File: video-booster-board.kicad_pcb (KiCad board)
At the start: 4 copper layers, 40 x 41.5 mm, 143 parts, among them IC1 INA180A1IDBVT, J1 0473460001, J10 M20-9990246, J12 solder_jumper, J13 solder_jumper, J14 solder_jumper, J2 CHDMI-AMSS-01-C-Vertical, J3 CHDMI-AMSS-01-C-Vertical, J4 694103107102, J5 solder_jumper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

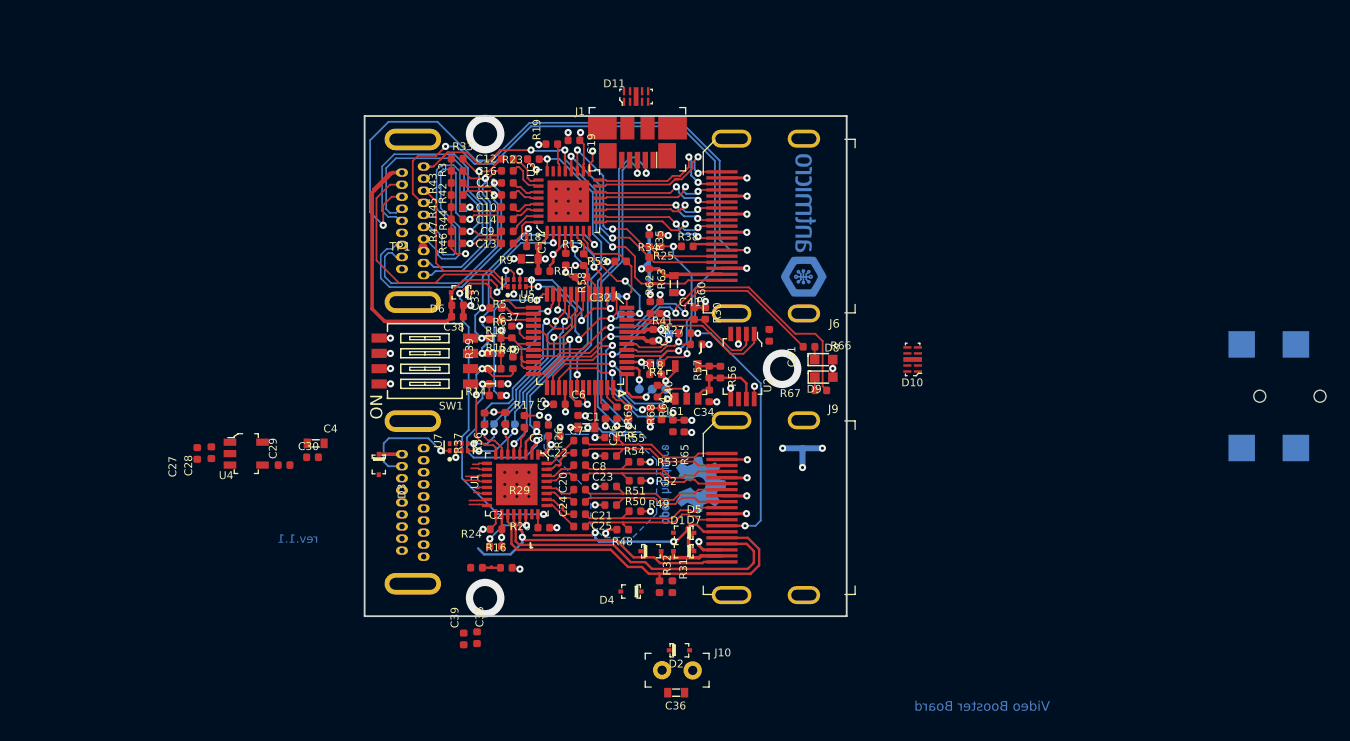
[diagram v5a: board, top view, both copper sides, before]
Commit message: Updated layout of 3V3 LDO
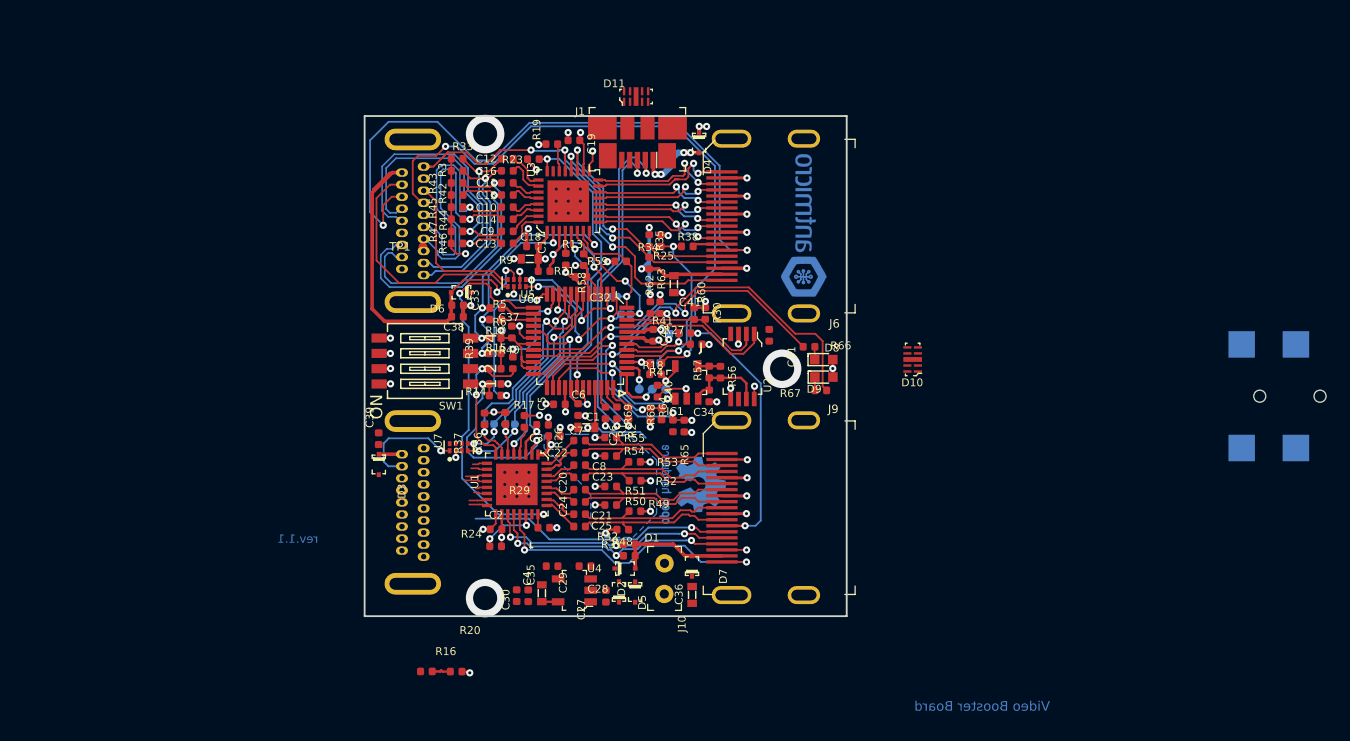
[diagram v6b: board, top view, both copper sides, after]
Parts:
- moved D4 37.7 mm to (137.8, 60.7), turned to 270 degrees
- moved C27 35.9 mm to (130.0, 98.3)
- moved C28 32.4 mm to (128.3, 95.8), turned to 180 degrees
- moved U4 29.5 mm to (127.4, 97.9), turned to 90 degrees
- moved C29 23.8 mm to (125.6, 95.8), turned to 180 degrees
- moved C4 22.5 mm to (124.7, 98.1), turned to 90 degrees
- moved C30 20.5 mm to (122.6, 98.3), turned to 90 degrees
- moved C39 18.0 mm to (111.2, 85.3)
- moved R16 9.56 mm to (115.1, 104.6)
- moved R20 9.56 mm to (117.6, 104.6)
- moved J10 8.87 mm to (134.9, 95.6), turned to 270 degrees
- moved C36 8.22 mm to (137.2, 98.2), turned to 270 degrees
- moved D5 7.28 mm to (131.1, 98.0), turned to 90 degrees
- moved D2 6.07 mm to (132.4, 98.0), turned to 270 degrees
- moved C35 5.49 mm to (123.6, 98.3)
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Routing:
- net /RX_SRC_SCL: track 29.9 -> 21.0 mm, vias 0 -> 3
- net /VUSB: track 9.09 -> 16.6 mm, vias 1 -> 5
- net /RX_SRC_SDA: track 27.1 -> 21.2 mm, vias 0 -> 3
- net GND: track 65.6 -> 60.4 mm, vias 45 -> 42
- net /RX_UTILITY: track 17.2 -> 21.7 mm, vias 2 -> 1
- net /RX_SRC_5V: track 6.10 -> 9.62 mm
- net +3V3: track 58.4 -> 59.6 mm
- net /TX_OUT_D2_P: track 13.5 -> 12.5 mm
- net /RX_HPD: track 24.2 -> 25.2 mm, vias 1 -> 2
- net /TX_OUT_D2_N: track 13.6 -> 12.7 mm
- net +5V: track 1.89 -> 1.12 mm, vias 0 -> 2
- removed copper zone on In2.Cu, net +3V3
- removed copper zone on In2.Cu, net /RX_SINK_5V
- removed copper zone on In2.Cu, net /TX_SRC_5V
- removed copper zone on In2.Cu, net GND

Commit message: Layout almost ready
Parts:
- removed J4: 694103107102, video-booster-board-footprints:69410X107102
- moved R20 23.5 mm to (115.7, 81.2), turned to 180 degrees
- moved R16 22.4 mm to (115.7, 82.1)
- moved D3 16.7 mm to (126.5, 94.0), turned to 0 degrees
- moved N1 9.48 mm to (146.5, 91.0)
- moved C31 0.75 mm to (143.4, 76.0)
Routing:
- net +5V: track 1.12 -> 38.6 mm, vias 2 -> 5
- net /TX_SRC_5V: track 39.4 -> 71.7 mm, vias 2 -> 5
- net +5VA: track 1.92 -> 32.5 mm, vias 2 -> 5
- net /VUSB: track 16.6 -> 43.6 mm
- net /RX_HPD: track 25.2 -> 50.7 mm, vias 2 -> 3
- net GND: track 60.4 -> 84.7 mm, vias 42 -> 54
- net /RX_SINK_CEC: track 5.96 -> 25.9 mm, vias 1 -> 3
- net /RX_OUT_CLK_P: track 1.51 -> 20.0 mm, vias 0 -> 1
- net /RX_OUT_D1_N: track 1.94 -> 20.3 mm, vias 0 -> 1
- net /RX_OUT_CLK_N: track 1.51 -> 19.5 mm, vias 0 -> 1
- net /RX_SINK_5V: track 2.07 -> 19.8 mm
- net /RX_OUT_D1_P: track 1.80 -> 19.5 mm, vias 0 -> 1
- net /RX_UTILITY: track 21.7 -> 39.4 mm, vias 1 -> 2
- net /TX_SINK_5V: track 18.1 -> 34.1 mm, vias 3 -> 5
- net /RX_SRC_5V: track 9.62 -> 25.4 mm, vias 0 -> 2
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- added copper zone on In2.Cu, net +3V3
- added copper zone on In2.Cu, net +5V
- added copper zone on In2.Cu, net +5VA
- added copper zone on In2.Cu, net /TX_SRC_5V

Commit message: Removed TVS, all signalls connected
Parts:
- removed D10, D11: RCLAMP0524PATCT_, video-booster-board-footprints:UFDFN-10_2.5x1mm
- moved C39 6.94 mm to (118.0, 84.1), turned to 180 degrees
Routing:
- net /RX_SINK_5V: track 19.8 -> 46.0 mm
- net /TX_SRC_5V: track 71.7 -> 73.2 mm
- net /RX_HPD: track 50.7 -> 49.9 mm
- net +3V3: track 67.4 -> 66.6 mm
- net /RX_SINK_CEC: track 25.9 -> 26.6 mm
- net /RX_EQ0: track 15.7 -> 16.3 mm
